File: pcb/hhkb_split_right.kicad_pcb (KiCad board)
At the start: 2 copper layers, 173.7 x 97.4 mm, 92 parts, among them SW1 6, SW10 Y, SW11 U, SW12 I, SW13 O, SW14 P, SW15 [, SW16 ], SW17 Del, SW18 H, SW19 J, SW2 7, SW20 K, SW21 L, SW22 ;, SW23 ', SW24 Enter, SW25 N, SW26 M, SW27 ,, SW28 ., SW29 /, SW3 8, SW30 Shift, SW31 Fn, SW32 R-Space, SW33 Meta, SW34 Alt, SW4 9, SW5 0, SW6 -, SW7 =, SW8 \, SW9 `, U1 74LVC595, U2 74LVC595

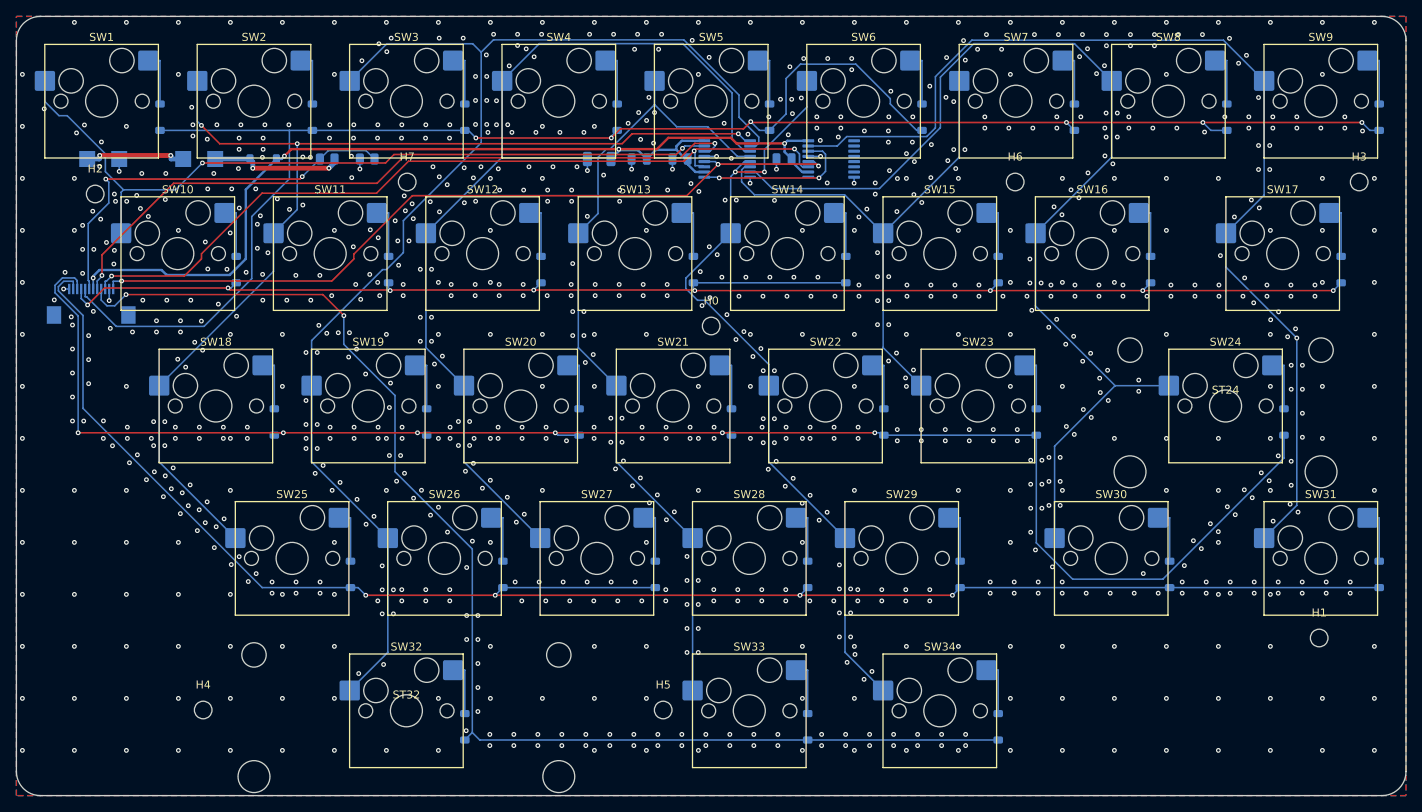
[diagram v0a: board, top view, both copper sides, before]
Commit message: C_RAIL を消した。置き場所の根拠が持たず C_U1 の重複だった
open-gaps #39 は「U1 の隣か J_DB の隣か」で止まっていたが、二択の
立て方が違った。FFC の反対側の C_DB を数えると、U_MCU から 3.95mm の
XIAO 用パスコンで、FFC 入口ではない。つまりケーブル入口のパスコンは
もともと両端どちらにも無く、片端だけ手当てする案は理屈が対称にならない。

C_RAIL は実測で J_DB から 70mm、C_U1 の 5.1mm 隣にあった（J_DB を
帯 1 へ移したときに取り残された）。名前どおりの役目は果たしていない。

消した理由は「不要と証明できたから」ではなく、必要と言える根拠が
1 つも無く、各 IC が既に自分の直近パスコンを持つから（595 は
C_U1/C_U2、XIAO は C_DB、レールは C_BULK）。

DRC 違反は左右子とも 0 のまま。右だけ未配線が 0 → 1 に増えた。中身は
信号線ではなく、(152.65, 68.37) の GND スティッチングビアがベタから
浮いたもの（C_RAIL の跡地）。自動配線 2 回で同じなので構造的。
配線に大きな変更が控えているため、それと併せて確認する（open-gaps #40）。

⚠️ pytest tools は最後まで通していない。次の配線変更とまとめて回す。

Co-Authored-By: Claude Opus 5 (1M context) <noreply@anthropic.com>
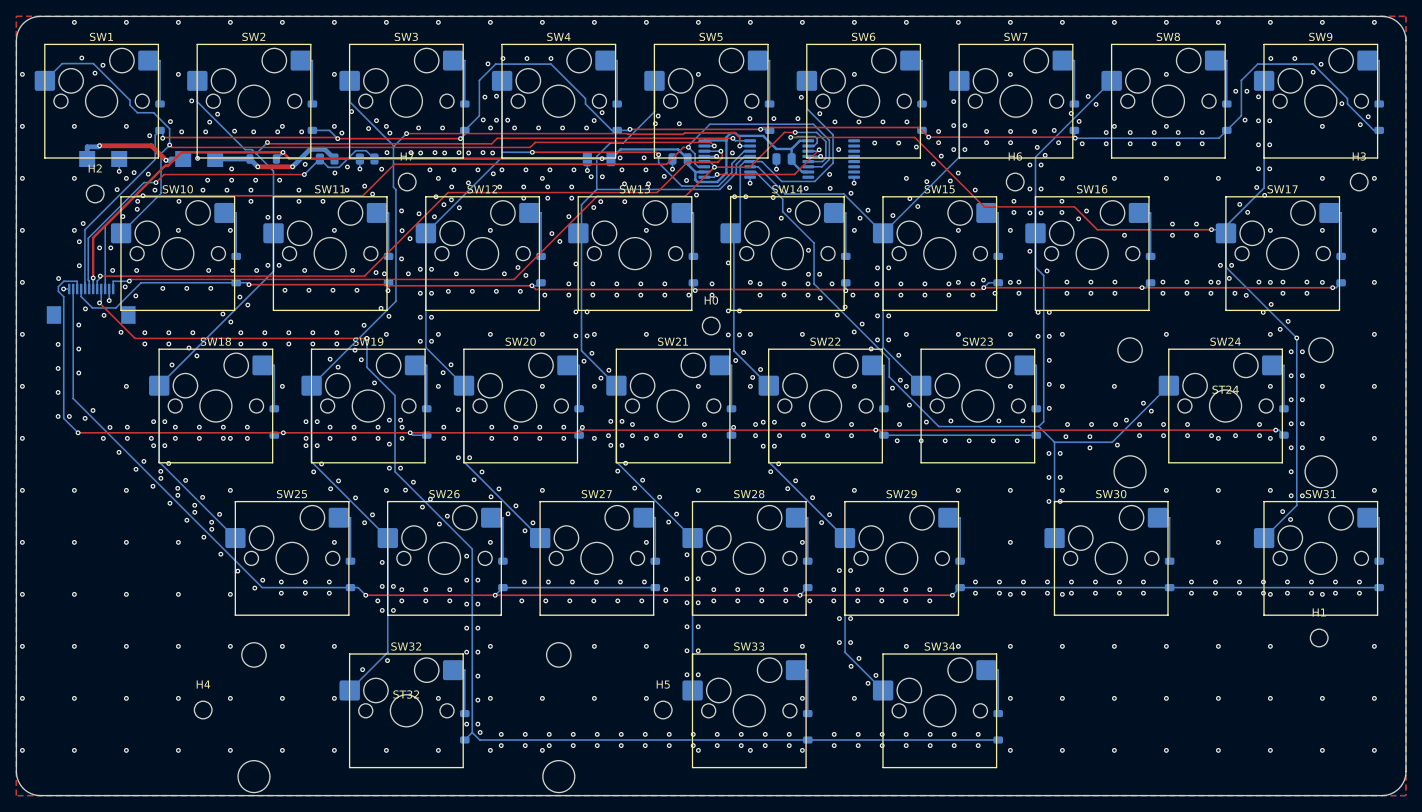
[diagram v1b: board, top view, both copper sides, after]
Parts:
- removed C_RAIL: cap_100n, C_0805_2012Metric
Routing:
- net ROW0: track 238.1 -> 205.5 mm, vias 6 -> 7
- net COL2: track 157.5 -> 135.5 mm, vias 0 -> 2
- net ROW1: track 187.0 -> 169.7 mm
- net SPI_SCK: track 100.8 -> 113.7 mm, vias 3 -> 2
- net V3V3: track 128.4 -> 119.3 mm, vias 4 -> 3
- net COL4: track 101.0 -> 108.6 mm
- net COL0: track 98.7 -> 105.7 mm
- net COL3: track 108.9 -> 102.8 mm, vias 0 -> 2
- net ROW2: track 206.2 -> 200.7 mm, vias 6 -> 7
- net CS: track 99.0 -> 104.3 mm
- net ROW3: track 213.5 -> 209.3 mm
- net COL8: track 132.8 -> 128.9 mm, vias 1 -> 3
- net COL6: track 67.1 -> 64.1 mm
- net U1_U2: track 20.0 -> 17.2 mm
- net VBATT_SENSE: track 50.5 -> 48.0 mm
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
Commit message: バルクを子基板へ移し、電源鎖を消費側へ寄せ、行バスを直線にした
利用者の指摘を順に潰した。どれも「測ったら前提が違っていた」型。

1. バルク（C_BULK）を子基板へ
   守る相手は XIAO の µs 級の電流変動（electrical-design 1-5）で、
   595 でも整流点でもない。XIAO は子基板にいるので、主基板に置くと
   FFC 100mm のインダクタンスの外側から供給することになる。
   XIAO の 3V3 パッドから 2.04mm の位置へ移した。

2. 電源ブロックを V3V3 の消費側へ
   整流点 D_PWR が板の左端にあるのに、消費側（C_U1・U1・J_DB）は
   全部反対側だった。U1 の左へ寄せて V3V3 の銅 132→81mm、
   VBATT_SENSE 110→78mm。左の帯 0 はアンテナ禁止域と取付穴で
   分断されていて、プラス側へは出せない（一度出して DRC 13 件）。

3. 行のバスを裏面の直線で自分で引く（prewire_row_bus）
   ROW0 が 222mm・ビア 7 本・区間 54 で表裏を行き来していた。
   同じ行のダイオードの K 側は y が完全に一致し、ライン上に
   スルーホールが無いので直線が引ける（ROW4 は元から 0 ビアだった）。
   左の未配線 1 本（ROW2）はこれで解決した。
   ⚠️ DSN に (autoroute_settings) を足す道は駄目。左が 66 本に壊れた。

4. アンテナの禁止域（30x15mm）を削除
   利用者の「本当にアンテナの真上ですか」で測ったら、覆っていなかった。
     禁止域 y 30.60..45.60 / 基板後端 48.70 / アンテナ 49.50..53.00
   アンテナは基板の後端より 0.80mm 奥（XIAO_OVERHANG 1.8mm の効果）で、
   平面的に基板の外。禁止域は 3.9mm 的を外したまま 450mm² を捨て、
   左の配線を圧迫していた。
   **根拠に挙げられていた検査は存在しなかった。**interface.py は
   test_the_antenna_keepout_actually_covers_the_antenna が照合すると
   書いていたが、その名前の検査はどこにも無い。実在したのは
   「禁止域の中が空か」だけで、位置は誰も見ていなかった。
   代わりに test_the_antenna_clears_the_main_board を置いた
   （XIAO_OVERHANG を 0 にすると落ちることを確認済み）。

   → open-gaps #23 の幾何の証明（アンテナは必ず 4mm 以上 基板の下に
     入る）は、もう成立していない。ただし余裕は 0.80mm しかないので、
     手 0（アルミ箔で RSSI）の価値は残る。#23 の書き直しは次。

残っているもの（次に着手する）:
  右 未配線 3（GND 離島 1 + V3V3 が J_DB へ届かない 2）★機能的な故障
  左 未配線 1（GND 離島）
  違反はどれも 0。自前配線で塞ぐ案は取らない——今は綺麗に引けても
  配置を変えると黙って壊れ、再現性が無い（利用者の判断）。

pytest tools は未実行。

Co-Authored-By: Claude Opus 5 (1M context) <noreply@anthropic.com>
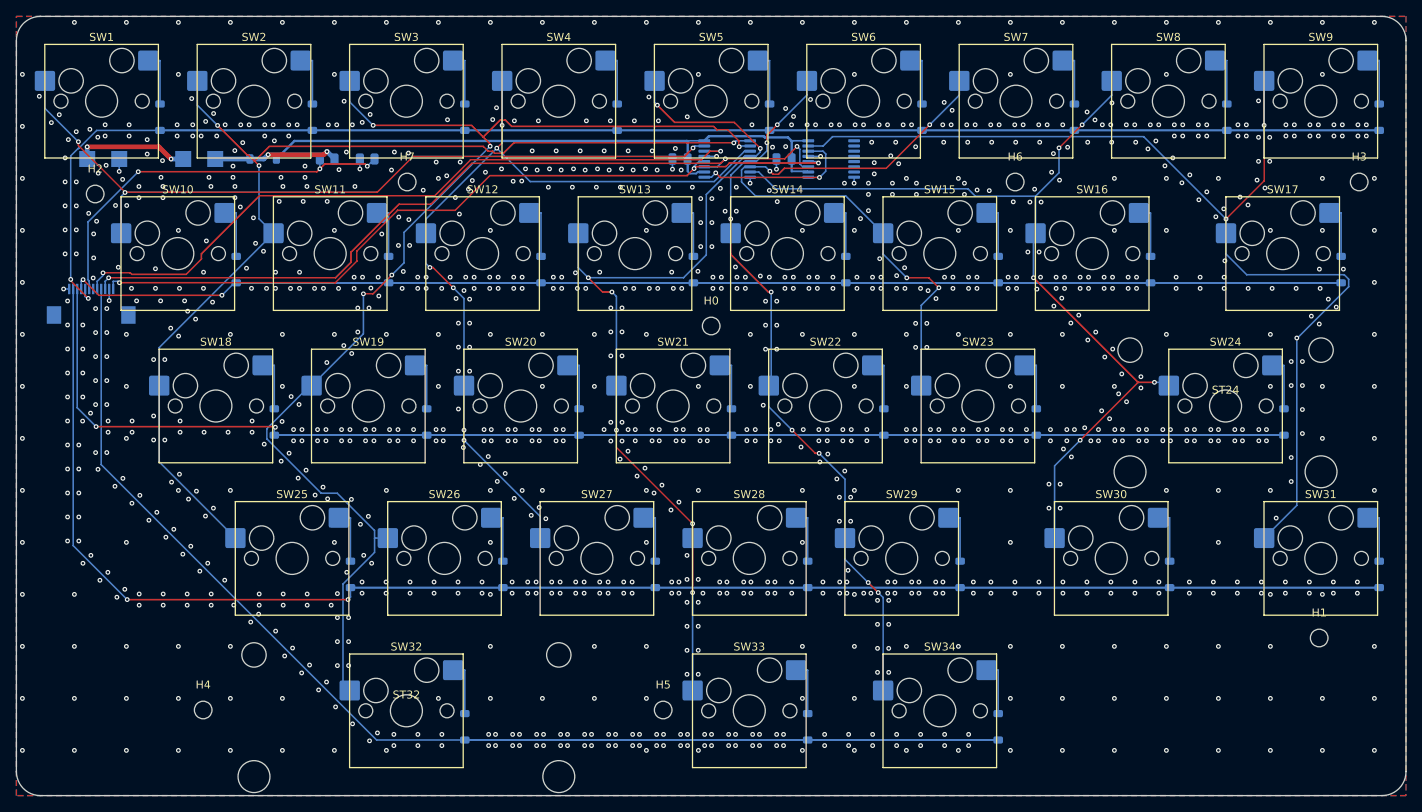
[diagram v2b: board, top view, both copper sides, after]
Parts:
- removed C_BULK: cap_100u, C_1206_3216Metric
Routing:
- net ROW0: track 205.5 -> 337.4 mm, vias 7 -> 2
- net ROW1: track 169.7 -> 298.1 mm, vias 8 -> 2
- net ROW3: track 209.3 -> 328.0 mm, vias 4 -> 2
- net ROW2: track 200.7 -> 294.1 mm, vias 7 -> 2
- net ROW4: track 159.3 -> 215.0 mm, vias 2 -> 0
- net V3V3: track 119.3 -> 79.9 mm, vias 3 -> 1
- net COL7: track 134.3 -> 111.9 mm, vias 0 -> 5
- net COL6: track 64.1 -> 80.0 mm, vias 0 -> 4
- net COL2: track 135.5 -> 149.5 mm, vias 2 -> 5
- net SPI_SCK: track 113.7 -> 101.8 mm, vias 2 -> 3
- net COL4: track 108.6 -> 116.7 mm, vias 0 -> 7
- net COL5: track 99.5 -> 91.4 mm, vias 0 -> 8
- net COL0: track 105.7 -> 98.2 mm, vias 2 -> 3
- net COL8: track 128.9 -> 134.0 mm
- net CS: track 104.3 -> 99.3 mm
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
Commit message: VBATT_RAW を廃止し、V3V3 を FFC の隙間を通る幅に直した
1. 電池の + を基板に通さない（利用者の指摘）
   BT1.+ →(VBATT_RAW)→ SW_PWR.1 と基板を往復させていたが、電池
   ボックスもスイッチもリード線で繋ぐので、+ はスイッチへ直接
   はんだ付けすればよい。線 4→3 本・ランド 4→2 個。基板から
   VBATT_RAW というネットが丸ごと消えた。
   ランドの数は WIRE_PAD_KINDS で 2 に決め打ちしていたのを、
   宣言した端子の数から取るように直した。参照名の接尾辞は端子数に
   関わらず付ける（1 個になった瞬間に BT1 へ化けて board_refs と
   回路図の配置表が一斉にずれるため）。

2. V3V3 の線幅 0.3 → 0.2mm ★右の V3V3 断線の真因
   「FFC の 0.30mm パッドに届く必要がある」と書いてあったが、
   **パッドの幅とパッドの隙間を取り違えていた。**0.5mm ピッチ・
   パッド幅 0.30 の列を幅 0.30 で抜けると隣のパッドまで 0.200mm
   ちょうどで、丸めで即割る（0.20mm なら 0.250mm で通る）。
   右基板で V3V3 だけが J_DB から出られず、自動配線器がビアだけ
   (72.75, 84.00) に置いて両端とも繋がず放棄していた。同じ列の
   VBATT_SENSE・SPI_MOSI・SCK・CS は全部 0.20mm で脱出できていた。
   電流は BLE のパルスで 15mA、バルクは子基板側なのでこの線が
   運ぶのは平均電流だけ。0.20mm でも桁が違うほど余る。

3. DSN のクリアランスマージン 15 → 20µm
   上の変更のあと 15 では丸め不足が顕在化し、違反が左 1・右 3 出た
   （実測 0.1917〜0.1919mm ＜ 0.2000mm）。20 で全部消える。
   15/20/25 の結果は autoroute.py に表で残した。

結果:
  左  違反 0 / 未配線 2
  右  違反 0 / 未配線 0   ← 今日はじめて 0/0
  子  違反 0 / 未配線 0

左の 2 本は ROW3/ROW4 が J_DB へ降りる枝。**瑣末と判断**（利用者）。
J_DB の ROW パッドの並び（ROW3,ROW2,ROW1,ROW0,ROW4）が行バスの
y 順と食い違っていて交差する。XIAO のピン割り当てを変えて順序を
揃えれば解ける見込み——次の課題。

pytest tools は未実行。

Co-Authored-By: Claude Opus 5 (1M context) <noreply@anthropic.com>
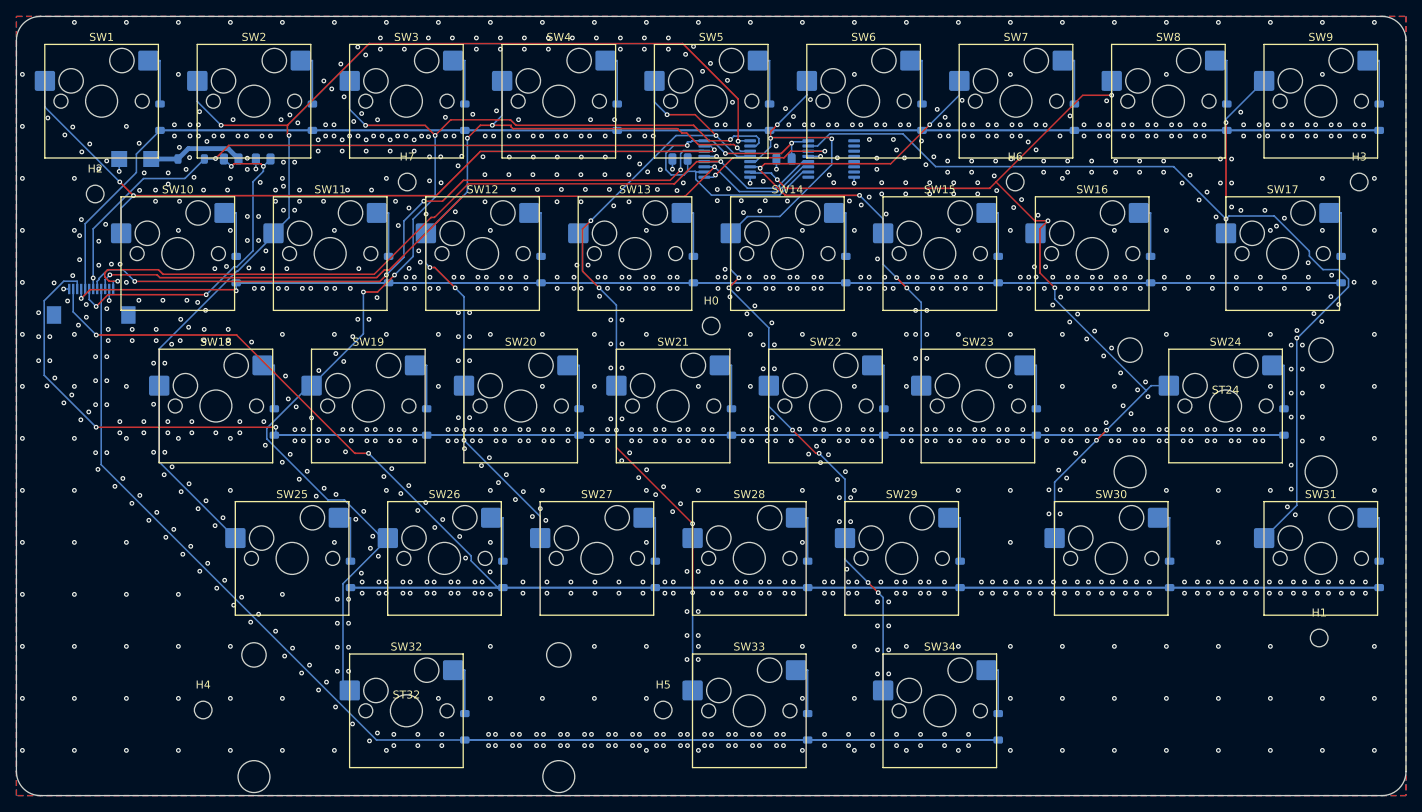
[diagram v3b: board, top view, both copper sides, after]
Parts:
- removed BT1_+: battery_holder, TestPoint_Pad_2.0x2.0mm
- removed SW_PWR_2: wire_pads, TestPoint_Pad_2.0x2.0mm
- moved R_LO 13.0 mm to (94.0, 69.1)
- moved R_HI 12.0 mm to (90.0, 69.1)
- moved D_PWR 9.00 mm to (85.0, 69.1)
- moved SW_PWR_1 4.00 mm to (80.0, 69.1)
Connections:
- SW_PWR_1 pad 1: VBATT_RAW -> VBATT_SW
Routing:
- net V3V3: track 79.9 -> 134.1 mm, vias 1 -> 5
- net ROW4: track 215.0 -> 238.8 mm
- net COL5: track 91.4 -> 106.9 mm, vias 8 -> 9
- net VBATT_RAW: track 14.1 -> 0.00 mm, vias 2 -> 0
- net COL1: track 134.7 -> 147.7 mm
- net COL4: track 116.7 -> 106.3 mm
- net ROW0: track 337.4 -> 328.5 mm, vias 2 -> 0
- net COL6: track 80.0 -> 72.7 mm, vias 4 -> 5
- net ROW2: track 294.1 -> 300.6 mm
- net VBATT_SENSE: track 49.0 -> 43.0 mm, vias 3 -> 4
- net COL7: track 111.9 -> 116.8 mm, vias 5 -> 6
- net VBATT_SW: track 15.7 -> 12.0 mm, vias 2 -> 0
- net CS: track 99.3 -> 102.9 mm, vias 3 -> 2
- net SPI_SCK: track 101.8 -> 99.0 mm, vias 3 -> 2
- net COL0: track 98.2 -> 100.7 mm
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
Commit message: 電源を子基板へ移し、FFC のピン順を両基板の都合から決め直した
利用者が絵を見ながら出した指摘を順に潰した回。**私は数字だけ見て
絵を見ておらず、同じ型の見落としを何度も拾ってもらった。**

■ 電源部を子基板へ（open-gaps #41）

  消費者は XIAO で、それは子基板にいる。起動と BLE 初期化で
  2.0〜2.5mA を継続、送信で 10〜15mA のパルス（task-c4-c5 測定 C /
  electrical-design 1-5）。595 の走査 100µA とは 100 倍以上ちがう。
  主基板で整流すると、その mA 級が FFC の 0.2mm 1 本を 100mm 渡る。

    FFC の V3V3   2.0〜2.5mA 継続 + パルス → **約 100µA**（150 分の 1）
    VBATT_SENSE   500kΩ が 100mm 渡る     → **渡らない**（ADC の 2mm 隣）
    ショットキー  隔離点まで FFC 100mm     → **3V3 パッド直近**
    主基板の帯    電源 5 点が SPI を塞ぐ   → **空いた**

  電池もスイッチも子基板のすぐ隣（実測: スイッチ→縁 左 4.0 / 右 20.7mm）
  なのでリード線はむしろ短くなる。

■ FFC のピン順（利用者「DB 単体でなく MAIN の都合も視野に入れて」）

  ROW0/1 は J_DB より上、ROW2/3/4 は下へ伸びる。行番号の昇順に並べると
  上下 2 群が必ず交差する（**実測 3 交差**）。群ごとに近い順で **0 交差**。
  そのズレは **XIAO のピン割り当て＝ファームで吸収**する（利用者の判断
  「配線でひねるのではなくソフトで受けるべき」）。

  ROW4 を D9 から左列へ戻した。右列へ逃がしていた理由は「左列が 6 本だと
  アンテナ直下を 2 本通る」だが、**その 6 本目は VBATT_SENSE だった。**
  分圧が子基板へ移って 5 本に戻ったので前提が消えた。
  → ファームの `&spi2_default`（MISO 外し）が**不要になり削除**。

■ アンテナの禁止域（利用者「こんなに広い必要ある？」「ズレてる」）

  子基板: 幅 18.3mm（XIAO の外形）を使っていた。**アンテナは 3.5mm 角**で
  4.1 倍。さらに y 方向に 2 つの細工（意味の無い切り詰めと水増し）があり、
  **アンテナの 57% しか覆っていなかった**。
    → `antenna_x_band()` に統一。**被覆 100%**、地板の無駄も消えた。
  主基板: アンテナから 3.9mm 外れた場所を抜いて 450mm² を捨てていた。
    → 削除（前のコミット）。

  ⚠️ **SES 往復でルール領域の層が消える**ことを発見した（GetLayer() が -1）。
  層を持たないゾーンは何も禁止しないので、あとから敷いたベタが
  アンテナ直下に入っていた（実測 3297 頂点）。`_restore_rule_area_layers`
  で戻す。**「宣言したから効いている」の 3 回目。**

■ 子基板を主基板と同じ水準に（利用者「MAIN にあって DB に無いもの」）

  両面 GND ベタ（裏面だけだった）・GND ファンアウト・スティッチング・
  離島の救済・電源のネットクラス。順序は **配置 → ネットクラス → 配線 →
  ベタ・ビア**（利用者「ベタは配線の残りで最大限やる」）。
  アンテナの禁止域だけは最初（配置と配線の制約なので）。

■ その他

  - バルクを縦置き＋向きを直した（V3V3/GND が XIAO と平行に並ぶ）
  - 行を D2〜D6 にして D1 を空け、奥側に 2.54mm 作った

■ 検査（どれも故意に壊して落ちることを確認）

  - `test_the_row_order_matches_between_firmware_and_circuit`
    行 N がファームと回路で同じピンを指すか。**既存の検査は集合しか
    見ておらず、D4 と D6 を入れ替えても通っていた**
  - 禁止域の寸法をアンテナの実寸と照合
  - `test_there_is_a_bulk_capacitor` を「XIAO と同じ基板にあるか」に
  - 変異検査が子基板も壊せるように（バルク移設で空振りしていた）
  - 正規表現がゾーンを跨いで**ベタ自身を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
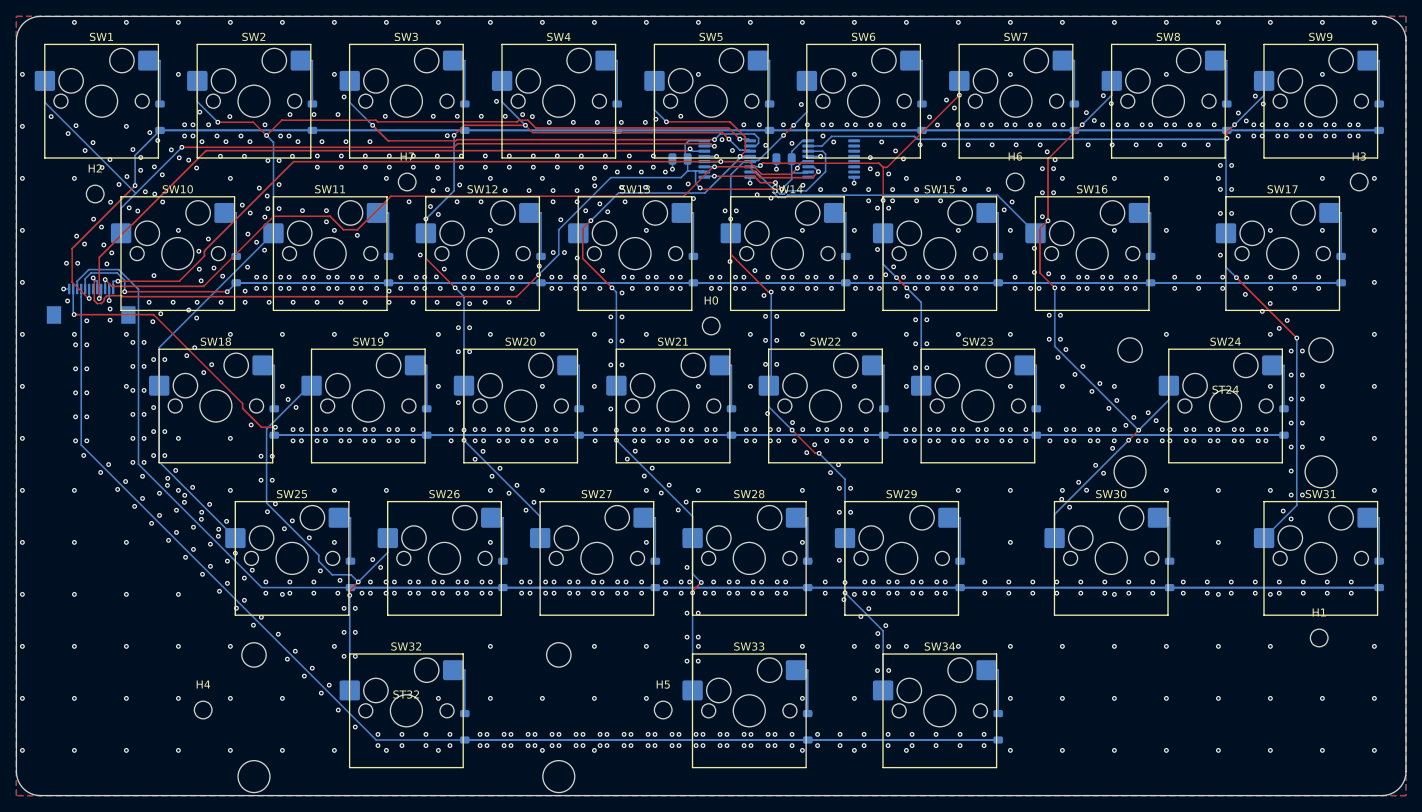
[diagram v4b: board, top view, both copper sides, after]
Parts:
- removed BT1_-: battery_holder, TestPoint_Pad_2.0x2.0mm
- removed D_PWR: schottky, D_SOD-123
- removed R_HI, R_LO: res_1M, R_0805_2012Metric
- removed SW_PWR_1: wire_pads, TestPoint_Pad_2.0x2.0mm
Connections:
- J_DB pad 10: ROW2 -> ROW3
- J_DB pad 11: ROW3 -> ROW2
- J_DB pad 4: ROW4 -> SPI_MOSI
- J_DB pad 5: SPI_MOSI -> V3V3
- J_DB pad 6: V3V3 -> (no net)
- J_DB pad 7: VBATT_SENSE -> ROW0
- J_DB pad 8: ROW0 -> ROW1
- J_DB pad 9: ROW1 -> ROW4
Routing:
- net VBATT_SENSE: track 43.0 -> 0.00 mm, vias 4 -> 0
- net COL2: track 149.7 -> 112.3 mm, vias 5 -> 4
- net COL8: track 134.2 -> 117.3 mm, vias 3 -> 4
- net V3V3: track 134.1 -> 118.6 mm, vias 5 -> 4
- net COL5: track 106.9 -> 91.5 mm, vias 9 -> 8
- net ROW2: track 300.6 -> 288.1 mm
- net VBATT_SW: track 12.0 -> 0.00 mm
- net COL1: track 147.7 -> 136.0 mm
- net COL6: track 72.7 -> 61.3 mm
- net ROW3: track 328.4 -> 322.2 mm, vias 2 -> 0
- net CS: track 102.9 -> 97.9 mm, vias 2 -> 3
- net COL4: track 106.3 -> 110.4 mm, vias 7 -> 8
- net ROW0: track 328.5 -> 332.5 mm, vias 0 -> 2
- net U1_U2: track 18.5 -> 22.3 mm
- net COL3: track 101.9 -> 105.1 mm
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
